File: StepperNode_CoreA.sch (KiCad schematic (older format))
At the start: 1 part

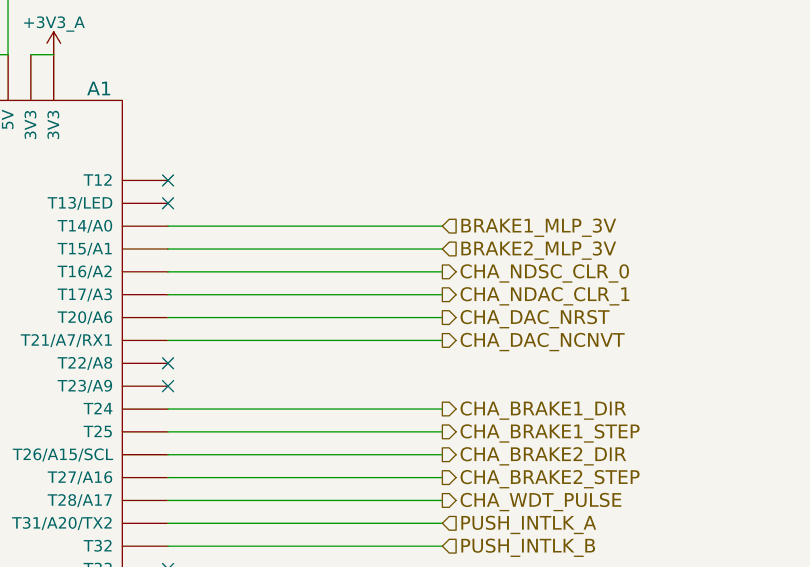
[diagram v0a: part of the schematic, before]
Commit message: Finish isolation and add brake limit switches.
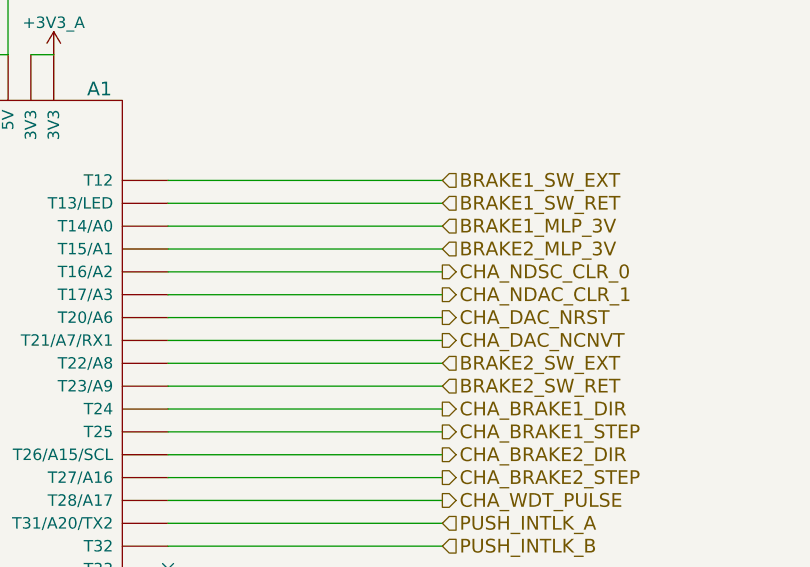
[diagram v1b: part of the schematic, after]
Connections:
- net BRAKE1_SW_EXT: now reaches A1.T12
- net BRAKE1_SW_RET: now reaches A1.T13 (T13/LED)
- net BRAKE2_SW_EXT: now reaches A1.T22 (T22/A8)
- net BRAKE2_SW_RET: now reaches A1.T23 (T23/A9)
- no-connect marks 19 -> 15
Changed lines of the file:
@@
 CHA_ACCEL2_NINT
 $Comp
-L +3V3_A #PWR020
+L +3V3_A #PWR63
 U 1 1 575DF18E
 P 8400 3050
-F 0 "#PWR020" H 8400 2900 50  0001 C CNN
+F 0 "#PWR63" H 8400 2900 50  0001 C CNN
 F 1 "+3V3_A" H 8400 3190 50  0000 C CNN
 F 2 "" H 8400 3050 60  0000 C CNN
@@
 $EndComp
 $Comp
-L +5V_A #PWR021
+L +5V_A #PWR61
 U 1 1 575DF1A4
 P 8200 2800
-F 0 "#PWR021" H 8200 2650 50  0001 C CNN
+F 0 "#PWR61" H 8200 2650 50  0001 C CNN
 F 1 "+5V_A" H 8200 2940 50  0000 C CNN
 F 2 "" H 8200 2800 60  0000 C CNN
@@
 $EndComp
 $Comp
-L +24V_A #PWR022
+L +24V_A #PWR59
 U 1 1 575DF1BA
 P 8000 2600
-F 0 "#PWR022" H 8000 2450 50  0001 C CNN
+F 0 "#PWR59" H 8000 2450 50  0001 C CNN
 F 1 "+24V_A" H 8000 2740 50  0000 C CNN
 F 2 "" H 8000 2600 60  0000 C CNN
@@
 	8300 3050 8400 3050
 $Comp
-L GNDD #PWR023
+L GNDD #PWR60
 U 1 1 575DF220
 P 8050 6300
-F 0 "#PWR023" H 8050 6050 50  0001 C CNN
+F 0 "#PWR60" H 8050 6050 50  0001 C CNN
 F 1 "GNDD" H 8050 6150 50  0000 C CNN
 F 2 "" H 8050 6300 50  0000 C CNN
@@
 IB_FR_RX_3V
 $Comp
-L GNDA #PWR024
+L GNDA #PWR62
 U 1 1 576218DF
 P 8250 6350
-F 0 "#PWR024" H 8250 6100 50  0001 C CNN
+F 0 "#PWR62" H 8250 6100 50  0001 C CNN
 F 1 "GNDA" H 8250 6200 50  0000 C CNN
 F 2 "" H 8250 6350 50  0000 C CNN
@@
 Wire Wire Line
 	8250 6300 8250 6350
-NoConn ~ 8900 3600
-NoConn ~ 8900 3700
-NoConn ~ 8900 4400
-NoConn ~ 8900 4500
 NoConn ~ 8900 5300
 NoConn ~ 8900 5800
@@
 NoConn ~ 8900 5600
 NoConn ~ 8900 5700
+Wire Wire Line
+	10100 3600 8900 3600
+Wire Wire Line
+	10100 3700 8900 3700
+Text HLabel 10100 3600 2    60   Input ~ 0
+BRAKE1_SW_EXT
+Text HLabel 10100 3700 2    60   Input ~ 0
+BRAKE1_SW_RET
+Wire Wire Line
+	10100 4400 8900 4400
+Wire Wire Line
+	10100 4500 8900 4500
+Text HLabel 10100 4400 2    60   Input ~ 0
+BRAKE2_SW_EXT
+Text HLabel 10100 4500 2    60   Input ~ 0
+BRAKE2_SW_RET
 $EndSCHEMATC
